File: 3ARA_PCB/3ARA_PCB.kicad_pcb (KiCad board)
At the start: 2 copper layers, 95 x 95 mm, 74 parts, among them J1 ST-LINK V2, J10 Encoder 2, J11 Encoder 3, J12 JUMP_1, J13 JUMP_2, J14 I2C 1, J15 UART 5, J16 GPIO, J2 Motor 1, J3 Hall 3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

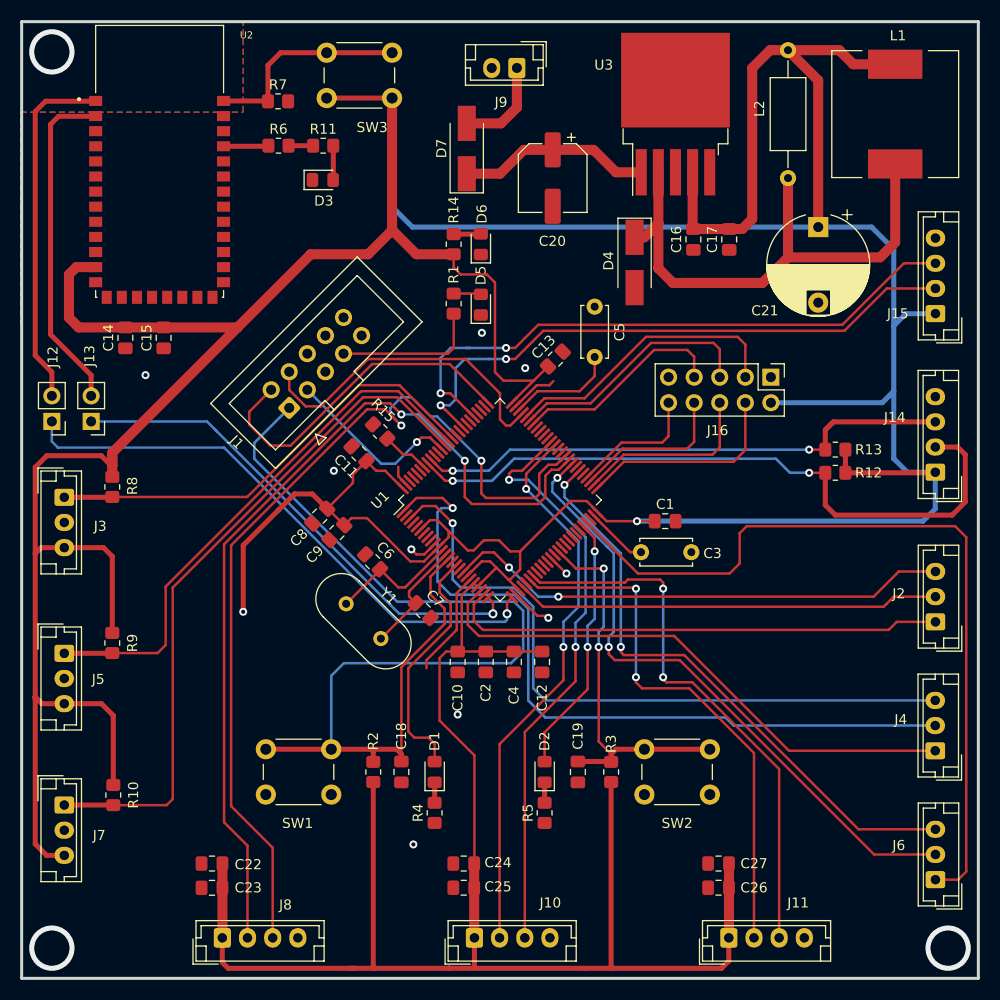
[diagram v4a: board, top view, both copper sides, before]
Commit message: Agregado de diseño 3D para HC05
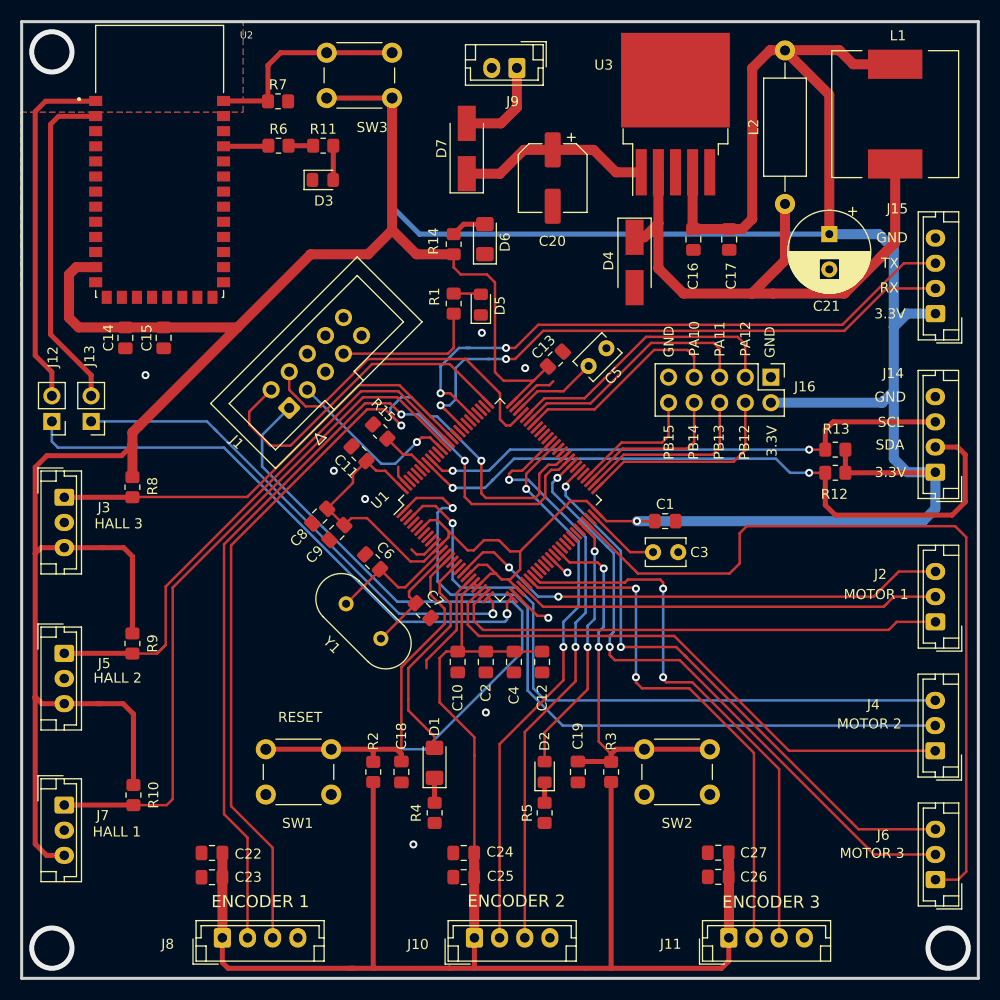
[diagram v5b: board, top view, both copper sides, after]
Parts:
- added G***: LOGO, Logo_UTN:LogoUTN, B.Cu at (119.1, 70.9)
- C21: footprint Capacitor_THT:CP_Radial_D10.0mm_P7.50mm -> Capacitor_THT:CP_Radial_D8.0mm_P3.50mm
- C3, C5: footprint Capacitor_THT:C_Disc_D5.0mm_W2.5mm_P5.00mm -> Capacitor_THT:C_Disc_D3.8mm_W2.6mm_P2.50mm
- D1, D6: footprint LED_SMD:LED_0805_2012Metric_Pad1.15x1.40mm_HandSolder -> LED_SMD:LED_1206_3216Metric_Pad1.42x1.75mm_HandSolder
- L2: footprint Inductor_THT:L_Axial_L7.0mm_D3.3mm_P12.70mm_Horizontal_Fastron_MICC -> Inductor_THT:L_Axial_L9.5mm_D4.0mm_P15.24mm_Horizontal_Fastron_SMCC
- R1: value 120 -> 1K
- moved L2 2.59 mm to (180.8, 68.1)
- moved R9 2.00 mm to (116.0, 111.8)
- moved R8 2.00 mm to (116.0, 96.2)
- moved R10 2.00 mm to (116.1, 126.8)
- moved C21 1.30 mm to (185.2, 71.1)
- moved C3 1.20 mm to (167.7, 102.7)
- moved C5 1.08 mm to (161.3, 84.2), turned to 45 degrees
- moved C26 1.08 mm to (174.2, 134.9)
- moved C27 1.08 mm to (174.2, 132.5)
- moved C25 1.05 mm to (148.9, 134.9)
- moved C22 1.05 mm to (123.9, 132.6)
- moved C23 1.05 mm to (123.9, 135.0)
- moved C24 1.05 mm to (148.9, 132.6)
- moved D1 0.90 mm to (146.0, 123.6)
- moved D6 0.64 mm to (151.0, 71.6)
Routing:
- net +3V3: track 660.4 -> 670.7 mm, vias 2 -> 1
- net Net-(D4-Pad1): track 53.9 -> 59.3 mm
- net /NRST: track 109.8 -> 104.8 mm
- net /PC1: track 24.3 -> 22.1 mm
- net Net-(C5-Pad1): track 10.8 -> 8.71 mm
- net /HALL_3: track 45.4 -> 47.4 mm
- net Net-(C3-Pad1): track 6.25 -> 7.41 mm
- net /HALL_2: track 54.5 -> 55.6 mm
- net Net-(D6-Pad2): track 2.71 -> 3.51 mm
- net /PB7_I2C1_SDA: track 67.8 -> 68.6 mm
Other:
- board text added: "3.3V"
- board text added: "ENCODER 1"
- board text added: "ENCODER 2"
- board text added: "ENCODER 3"
- board text added: "GND"
- board text added: "HALL 1"
- board text added: "HALL 2"
- board text added: "HALL 3"
- board text added: "Ignacio J. Cipolatti"
- board text added: "MOTOR 1"
- board text added: "MOTOR 2"
- board text added: "MOTOR 3"
- board text added: "PA10"
- board text added: "PA11"
- board text added: "PA12"
- board text added: "PB12"
- board text added: "PB13"
- board text added: "PB14"
- board text added: "PB15"
- board text added: "RESET"
- board text added: "RX"
- board text added: "SCL"
- board text added: "SDA"
- board text added: "TX"
